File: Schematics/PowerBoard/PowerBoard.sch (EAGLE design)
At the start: 22 parts

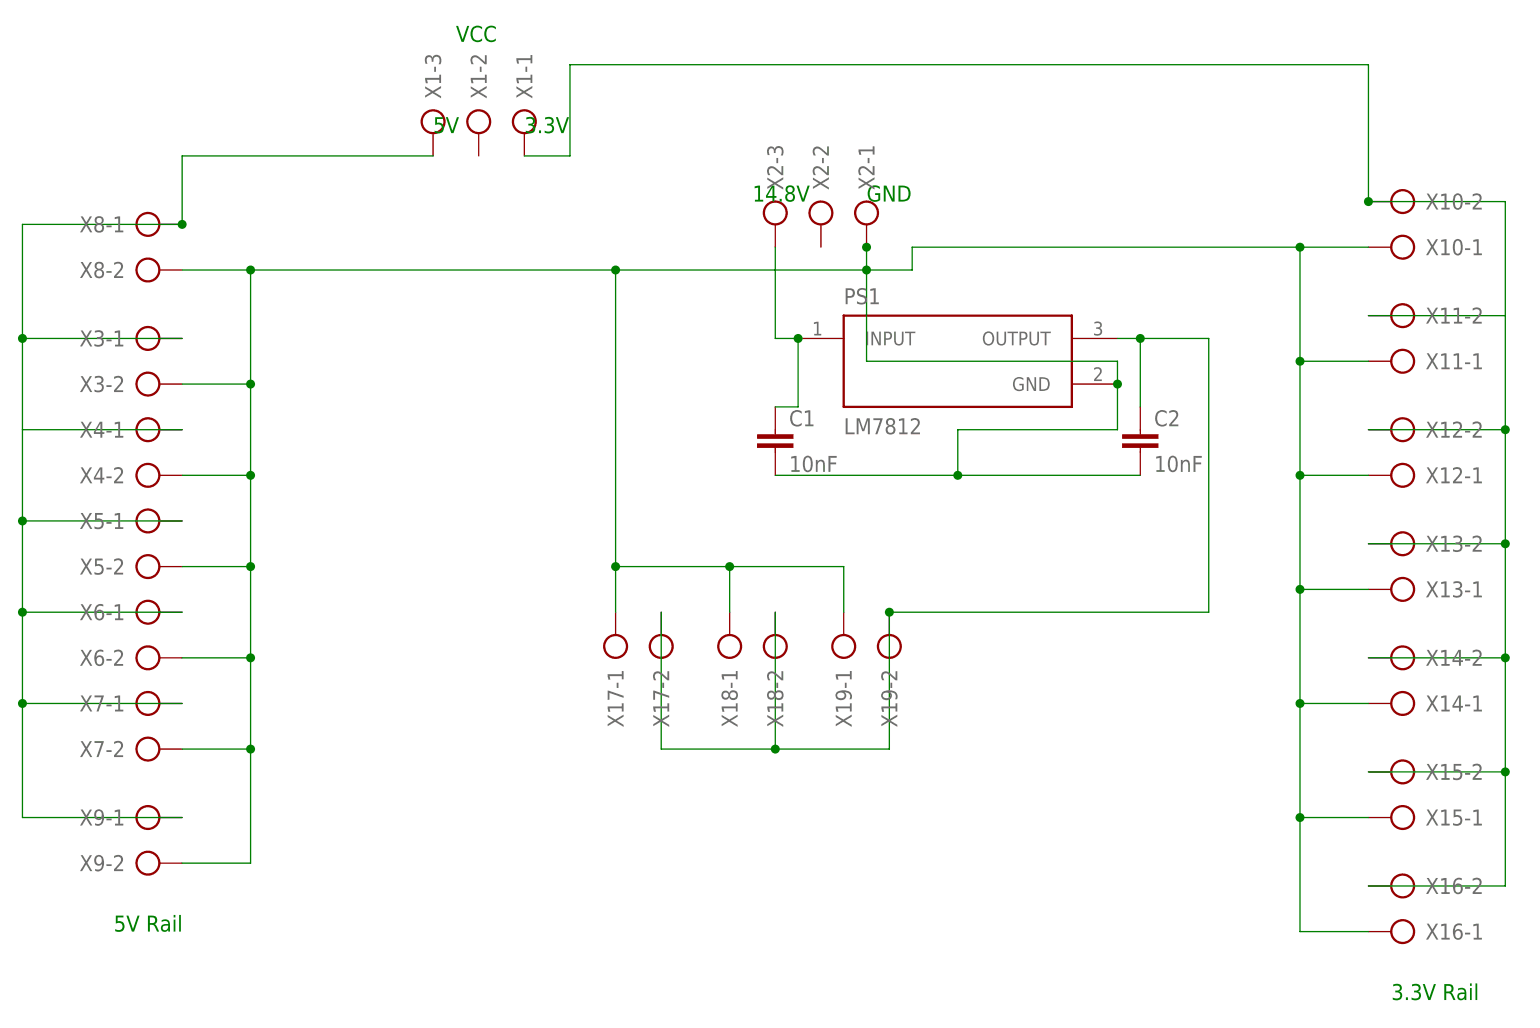
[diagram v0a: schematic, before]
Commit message: Refactored Power PCB
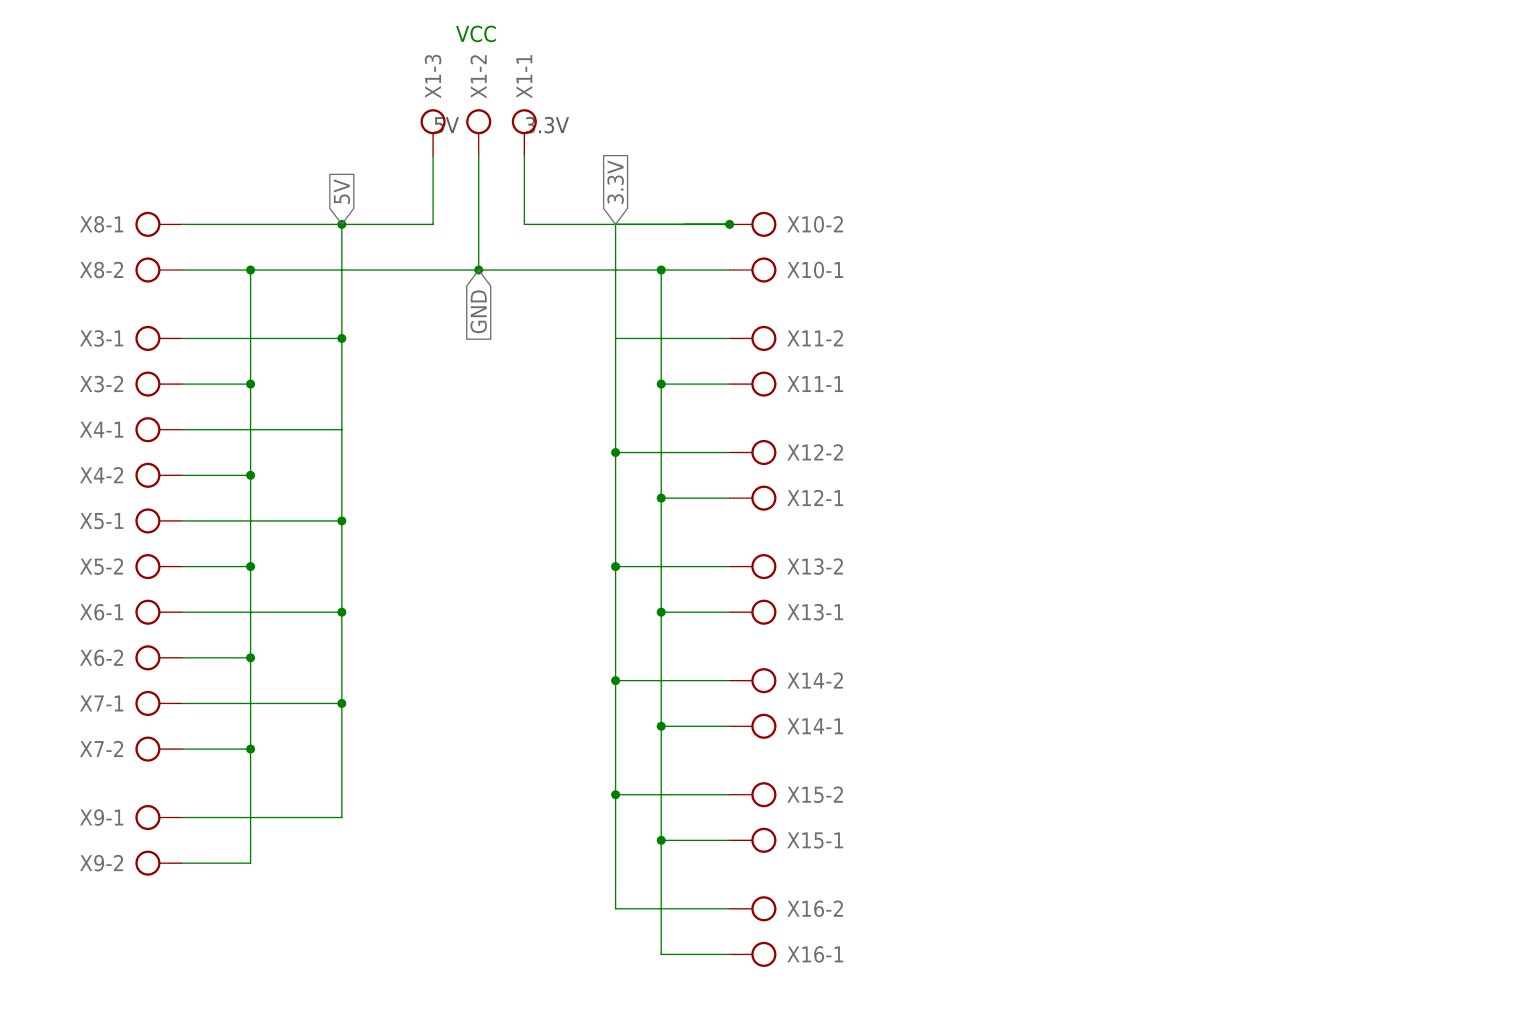
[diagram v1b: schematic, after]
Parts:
- removed C1, C2: 10nF, SparkFun-Capacitors:10NF-PTH-10MM-10000V-1-%
- removed PS1: LM7812, LM7812:LM7812
- removed X17, X18, X19: (no value), con-ptr500:AK500/2
- removed X2: (no value), con-ptr500:AK500/3
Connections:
- net N$3 renamed 5V
- net N$5 renamed 3.3V
- removed net N$1: C1.1, PS1.INPUT, X2-3.KL
- removed net N$2: C1.2, C2.2, PS1.GND, X10-1.KL, X11-1.KL, X12-1.KL, X13-1.KL, X14-1.KL, X15-1.KL, X16-1.KL, X17-1.KL, X18-1.KL, X19-1.KL, X2-1.KL, X3-2.KL, X4-2.KL, X5-2.KL, X6-2.KL, X7-2.KL, X8-2.KL, X9-2.KL
- removed net N$4: C2.1, PS1.OUTPUT, X17-2.KL, X18-2.KL, X19-2.KL
- new net GND: X1-2.KL, X10-1.KL, X11-1.KL, X12-1.KL, X13-1.KL, X14-1.KL, X15-1.KL, X16-1.KL, X3-2.KL, X4-2.KL, X5-2.KL, X6-2.KL, X7-2.KL, X8-2.KL, X9-2.KL
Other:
- note removed: "14.8V"
- note removed: "3.3V Rail"
- note removed: "5V Rail"
- note removed: "GND"
- moved on the sheet: X10-1, X10-2, X11-1, X11-2, X12-1, X12-2, X13-1, X13-2, X14-1, X14-2, X15-1, X15-2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
